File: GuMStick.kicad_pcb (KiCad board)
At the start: 2 copper layers, 20 x 66.2 mm, 31 parts, among them Q1 AO3401A, U1 XIAO-nRF52840-SMD, U2 Wio-SX1262, U3 HX PM2.54-1X4P WT, U5 BQ25606RGER

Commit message: Update file names, add Seeed X Meshtastic silkscreen
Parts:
- added G***: LOGO, LOGO, B.Cu at (142.1, 119.3)

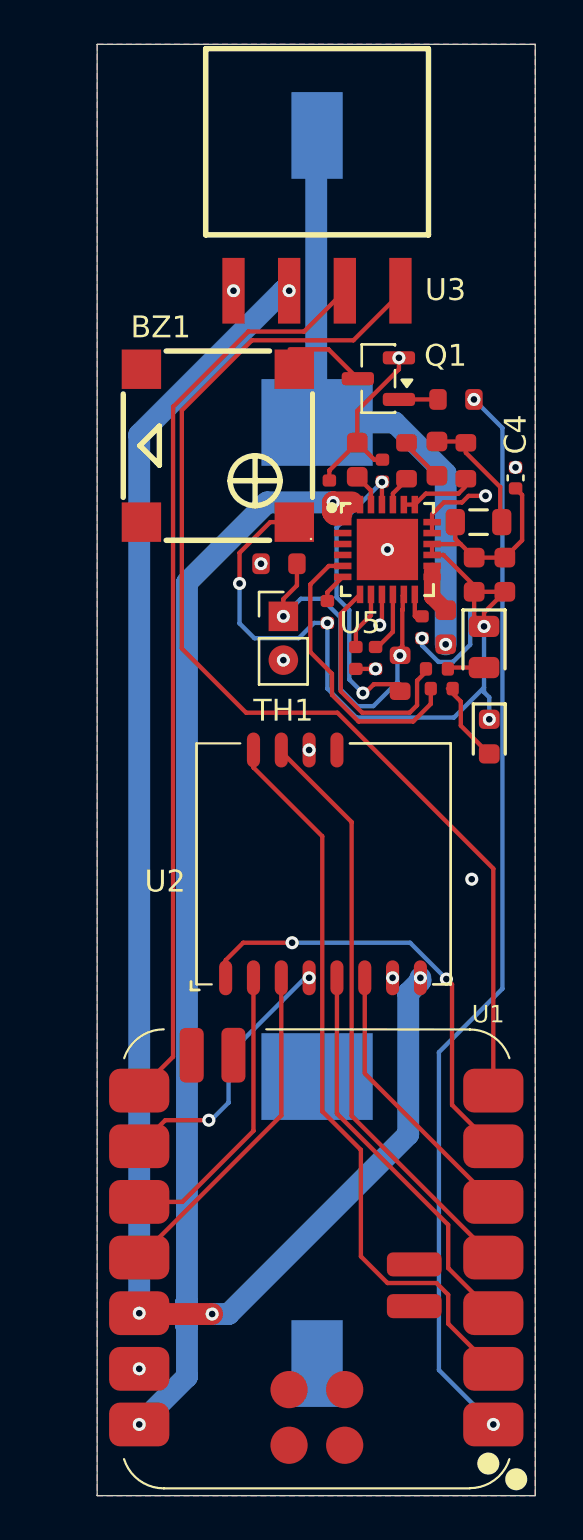
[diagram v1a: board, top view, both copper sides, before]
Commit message: Schematic changes, PCB changes not yet complete. Removed error with debounce capacitor in series with Bat+, should have been parallel, prevented system from working. Added a second mosfet for reverse polarity protection (learned to put that in the hard way). Increased RICHG resistor value to lower the charging current to 1A, the battery was getting warm while charging. Future PCB changes will reflect this and move the thermistor pads to the back of the board where they're easier to access for soldering.
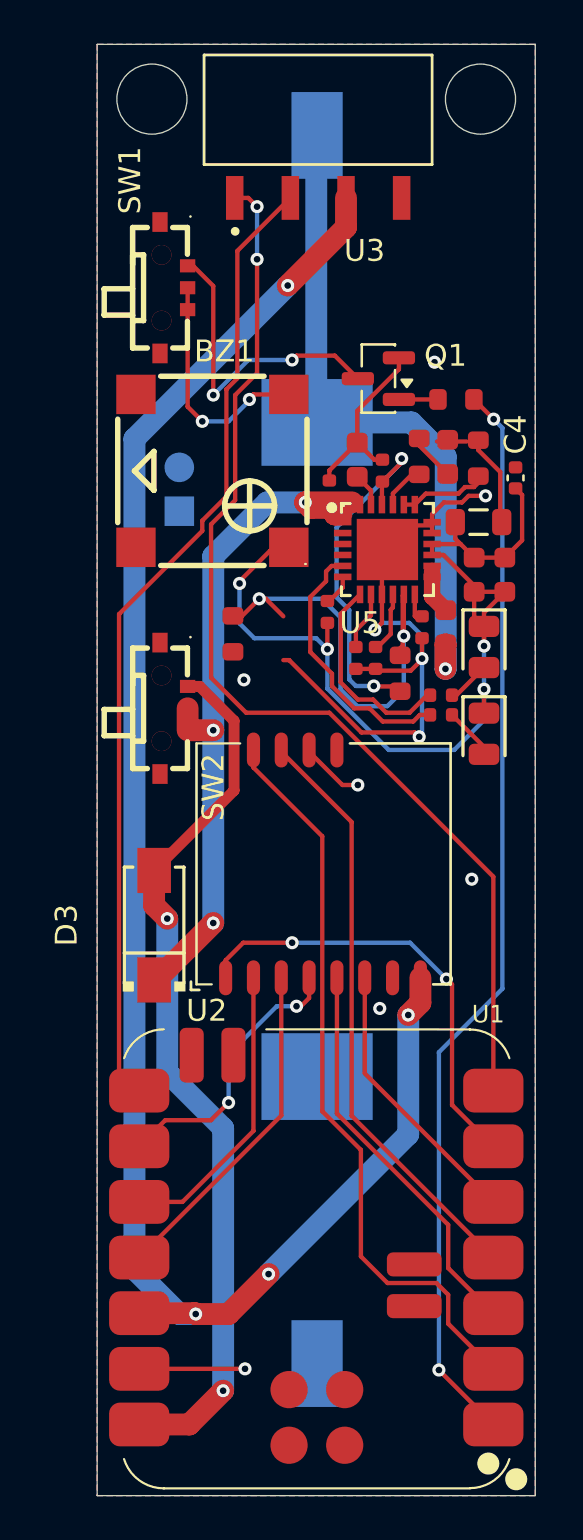
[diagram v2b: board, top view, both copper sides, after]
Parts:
- added D3: SS54_C22452, easyeda2kicad:SMA_L4.4-W2.8-LS5.4-R-RD, F.Cu at (142.6, 119.5)
- added SW1: K3-1235S, easyeda2kicad:SW-SMD_MK-11C04-G013, F.Cu at (143.5, 90.4)
- added SW2: K3-1235S, easyeda2kicad:SW-SMD_MK-11C04-G013, F.Cu at (143.5, 109.6)
- BAT+1: renamed from BAT1; footprint easyeda2kicad:BAT-SMD_MY-AAA-06 -> easyeda2kicad:BAT-SMD_MY-AA-04
- BAT-1: renamed from BAT2; footprint easyeda2kicad:BAT-SMD_MY-AAA-06 -> easyeda2kicad:BAT-SMD_MY-AA-04
- D1: footprint PCM_JLCPCB:D_0603 -> PCM_JLCPCB:D_0805
- Q1: value AO3401A -> SI2302
- TH1: moved to B.Cu
- U3: value HX PM2.54-1X4P WT -> M20-7910442R; footprint easyeda2kicad:CONN-SMD_4P-P2.54_HX-PM2.54-1X4PWT -> M20_7910442R 4 pin Header:MF254RS-11-04-0743 XFCN 4 Pin Machined Header
- moved G*** 18.6 mm to (158.1, 109.6)
- moved U3 7.06 mm to (150.1, 83.5), turned to 0 degrees
- moved TH1 6.75 mm to (143.8, 100.6)
- moved R18 3.83 mm to (146.2, 106.2), turned to -90 degrees
- moved R13 1.21 mm to (155.7, 109.0)
- moved R14 1.20 mm to (155.7, 109.9)
- moved BZ1 1.18 mm to (145.3, 98.8)
- moved R17 0.61 mm to (154.7, 98.1)
- moved R16 0.58 mm to (157.4, 98.2)
- moved C6 0.50 mm to (156.0, 98.1)
- moved D1 0.27 mm to (157.7, 110.8)
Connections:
- BZ1 pad 2: Net-(Q1-D) -> Net-(BZ1-Pad2)
- U1 pad 14: VBUS -> Net-(D3-A)
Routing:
- net Net-(D3-A): track 0.00 -> 40.6 mm, vias 0 -> 2
- net GND: track 18.9 -> 45.3 mm, vias 14 -> 10
- net VBUS: track 49.3 -> 32.0 mm, vias 2 -> 3
- net Net-(BZ1-Pad2): track 0.00 -> 11.1 mm, vias 0 -> 2
- net Net-(Q1-D): track 3.67 -> 14.4 mm, vias 0 -> 2
- net 3V3: track 72.7 -> 79.6 mm
- net Net-(U5-TS): track 17.0 -> 21.3 mm
- net REGN: track 13.9 -> 16.7 mm
- net BAT+: track 27.8 -> 30.5 mm
- net SCL: track 41.9 -> 44.4 mm
- net SDA: track 52.0 -> 50.0 mm, vias 0 -> 2
- net Net-(U5-~{PG}): track 10.6 -> 9.37 mm
- net Net-(U5-STAT): track 13.3 -> 12.1 mm
- net SYS: track 43.4 -> 44.6 mm
- net Net-(U5-BTST): track 1.39 -> 2.40 mm
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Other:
- outline, holes or cut-outs redrawn
